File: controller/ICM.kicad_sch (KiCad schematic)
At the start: 52 parts, among them J1 QWIIC_CONNECTORJS-1MM, J2 QWIIC_CONNECTORJS-1MM, J3 CONN_06NO_SILK_NO_POP, J4 CONN_06NO_SILK_NO_POP, Q10 MOSFET-NCH-RE1C002UN, Q11 MOSFET-NCH-RE1C002UN, Q4 MOSFET-NCH-RE1C002UN, Q5 MOSFET-NCH-RE1C002UN, Q6 MOSFET-NCH-RE1C002UN, Q7 MOSFET-NCH-RE1C002UN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

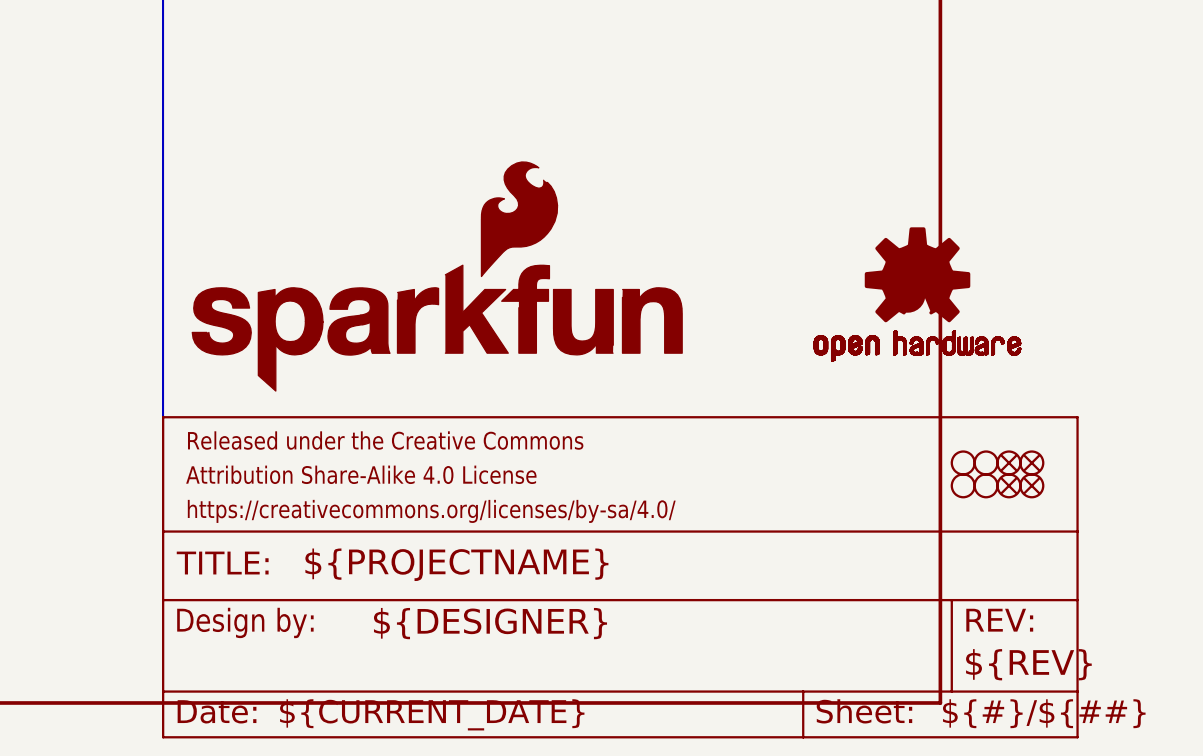
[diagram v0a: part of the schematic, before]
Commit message: changed hierarchy
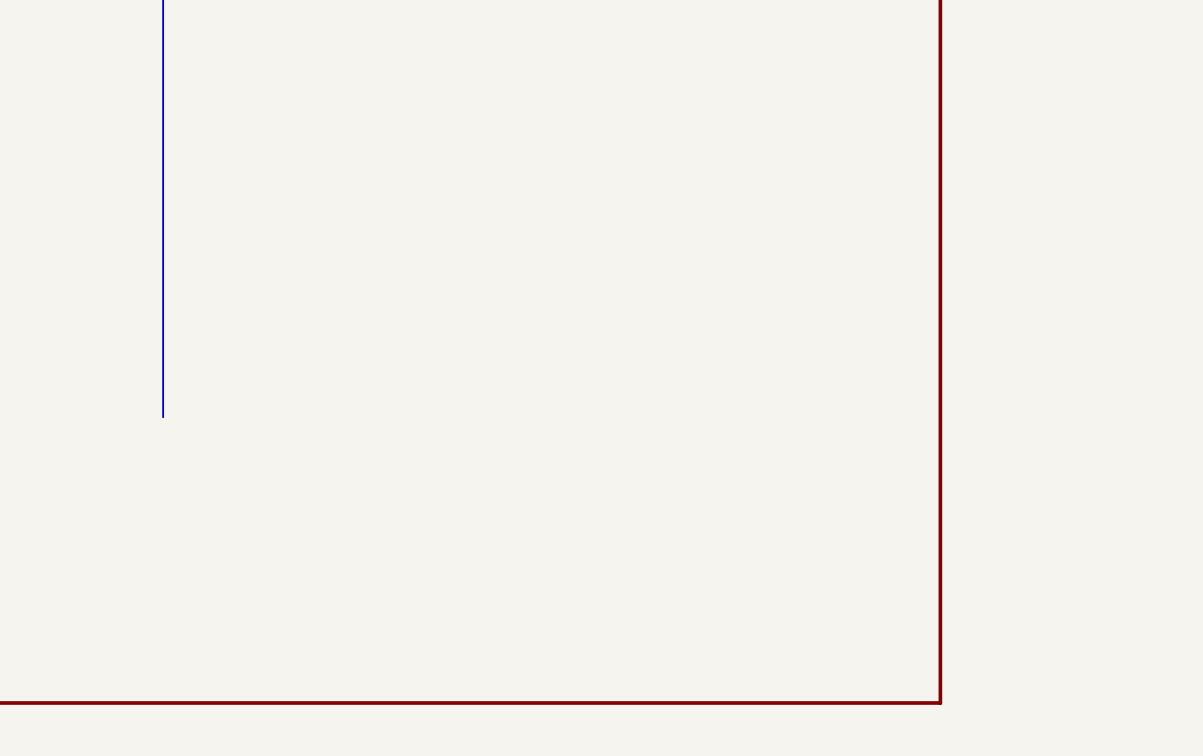
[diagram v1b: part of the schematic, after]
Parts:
- removed FD1, FD2, FD3, FD4: FIDUCIAL1X2, SparkFun_IMU_Breakout_ICM-20948:FIDUCIAL-1X2, symbol SparkFun_IMU_Breakout_ICM-20948-eagle-import:FIDUCIAL1X2
- removed unit 2 of FRAME1
- removed H1, H2, H3, H4: STAND-OFF, SparkFun_IMU_Breakout_ICM-20948:STAND-OFF, symbol SparkFun_IMU_Breakout_ICM-20948-eagle-import:STAND-OFF
- removed LOGO1: SFE_LOGO_NAME_FLAME.1_INCH, SparkFun_IMU_Breakout_ICM-20948:SFE_LOGO_NAME_FLAME_.1, symbol SparkFun_IMU_Breakout_ICM-20948-eagle-import:SFE_LOGO_NAME_FLAME.1_INCH
- removed LOGO2: OSHW-LOGOMINI, SparkFun_IMU_Breakout_ICM-20948:OSHW-LOGO-MINI, symbol SparkFun_IMU_Breakout_ICM-20948-eagle-import:OSHW-LOGOMINI

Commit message: finished ICM
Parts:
- removed J1, J2: QWIIC_CONNECTORJS-1MM, SparkFun_IMU_Breakout_ICM-20948:JST04_1MM_RA, symbol SparkFun_IMU_Breakout_ICM-20948-eagle-import:QWIIC_CONNECTORJS-1MM
- removed J3, J4: CONN_06NO_SILK_NO_POP, SparkFun_IMU_Breakout_ICM-20948:1X06_NO_SILK, symbol SparkFun_IMU_Breakout_ICM-20948-eagle-import:CONN_06NO_SILK_NO_POP
- removed JP4: JUMPER-SMT_3_2-NC_TRACE_SILK, SparkFun_IMU_Breakout_ICM-20948:SMT-JUMPER_3_2-NC_TRACE_SILK, symbol SparkFun_IMU_Breakout_ICM-20948-eagle-import:JUMPER-SMT_3_2-NC_TRACE_SILK
- removed JP5: JUMPER-SMT_2_NO_SILK, SparkFun_IMU_Breakout_ICM-20948:SMT-JUMPER_2_NO_SILK, symbol SparkFun_IMU_Breakout_ICM-20948-eagle-import:JUMPER-SMT_2_NO_SILK
- removed Q4, Q6: MOSFET-NCH-RE1C002UN, SparkFun_IMU_Breakout_ICM-20948:SOT-416FL, symbol SparkFun_IMU_Breakout_ICM-20948-eagle-import:MOSFET-NCH-RE1C002UN
- removed R14, R16, R5, R6: 2.2KOHM-0402T-1/16W-1%, SparkFun_IMU_Breakout_ICM-20948:0402-TIGHT, symbol SparkFun_IMU_Breakout_ICM-20948-eagle-import:2.2KOHM-0402T-1/16W-1%
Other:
- note removed: "ADR -> I2C Address ------------------- open -> 0x69 closed -> 0x68 *Closing AD0 precludes SPI"
- note removed: "Address Option"
- note removed: "Connections"
- note removed: "I2C Level Shifting + Pullup Disconnects"
- note removed: "Optionally disconnect the I2C pullup resistors on the primary and auxillary busses in case of too strong pullup from other sources"
- moved on the sheet: JP6, Q11, Q9, R19, R21, R23, R25
